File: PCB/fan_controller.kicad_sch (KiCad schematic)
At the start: 26 parts, among them IC17 LM393DR, J7 171825-2, M1 FFB0412VHN-B, Q2 SQ2348ES-T1_BE3

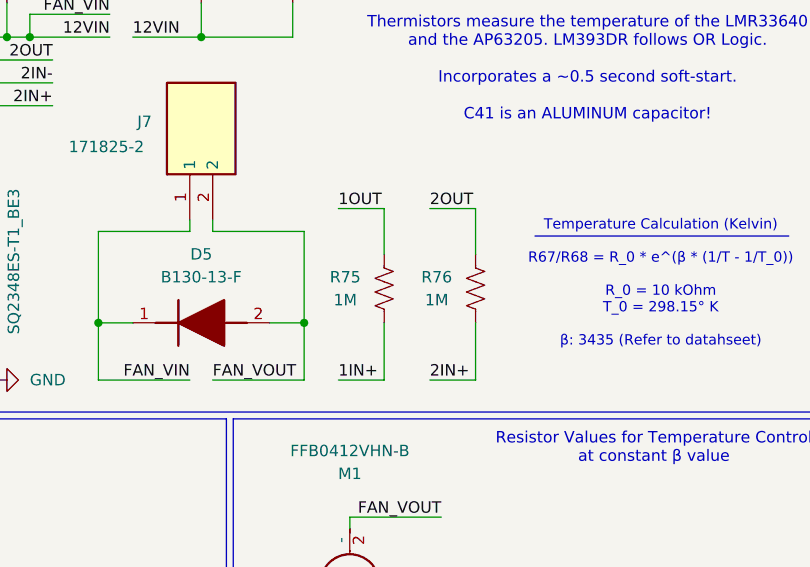
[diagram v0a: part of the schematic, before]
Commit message: Diagnosing Ethernet Controller
The Ethernet chip is dead, we'll need a new one. Minor optimizations everywhere.
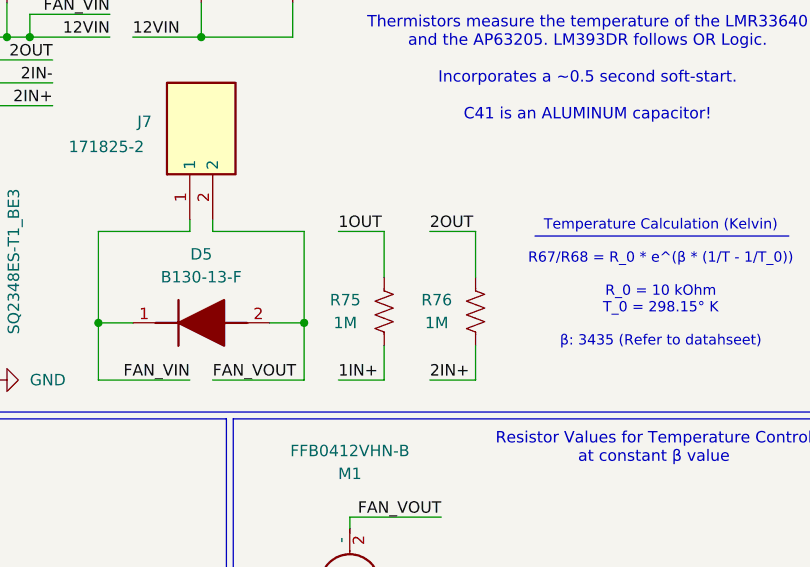
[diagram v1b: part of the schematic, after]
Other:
- moved on the sheet: R75, R76
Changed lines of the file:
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@@
 	(wire
 		(pts
-			(xy 148.59 49.53) (xy 153.67 49.53)
+			(xy 148.59 52.07) (xy 153.67 52.07)
 		)
 		(stroke
@@
 	(wire
 		(pts
-			(xy 153.67 62.23) (xy 153.67 68.58)
+			(xy 153.67 64.77) (xy 153.67 68.58)
 		)
 		(stroke
@@
 	(wire
 		(pts
-			(xy 143.51 62.23) (xy 143.51 68.58)
+			(xy 143.51 64.77) (xy 143.51 68.58)
 		)
 		(stroke
@@
 	(wire
 		(pts
-			(xy 143.51 49.53) (xy 143.51 54.61)
+			(xy 143.51 52.07) (xy 143.51 57.15)
 		)
 		(stroke
@@
 	(wire
 		(pts
-			(xy 153.67 49.53) (xy 153.67 54.61)
+			(xy 153.67 52.07) (xy 153.67 57.15)
 		)
 		(stroke
@@
 	(wire
 		(pts
-			(xy 138.43 49.53) (xy 143.51 49.53)
+			(xy 138.43 52.07) (xy 143.51 52.07)
 		)
 		(stroke
@@
 	)
 	(label "1OUT"
-		(at 138.43 49.53 0)
+		(at 138.43 52.07 0)
 		(effects
 			(font
@@
 	)
 	(label "2OUT"
-		(at 148.59 49.53 0)
+		(at 148.59 52.07 0)
 		(effects
 			(font
@@
 	(symbol
 		(lib_id "Device:R_US")
-		(at 143.51 58.42 180)
+		(at 143.51 60.96 180)
 		(unit 1)
 		(body_style 1)
@@
 		(dnp no)
 		(property "Reference" "R75"
-			(at 139.192 57.15 0)
+			(at 139.192 59.69 0)
 			(show_name no)
 			(do_not_autoplace no)
@@
 		)
 		(property "Value" "1M"
-			(at 139.192 59.69 0)
+			(at 139.192 62.23 0)
 			(show_name no)
 			(do_not_autoplace no)
@@
 		)
 		(property "Footprint" "Resistor_SMD:R_0805_2012Metric_Pad1.20x1.40mm_HandSolder"
-			(at 142.494 58.166 90)
+			(at 142.494 60.706 90)
 			(hide yes)
 			(show_name no)
@@
 		)
 		(property "Datasheet" ""
-			(at 143.51 58.42 0)
+			(at 143.51 60.96 0)
 			(hide yes)
 			(show_name no)
@@
 		)
 		(property "Description" "Resistor, US symbol"
-			(at 143.51 58.42 0)
+			(at 143.51 60.96 0)
 			(hide yes)
 			(show_name no)
@@
 		)
 		(property "Manufacturer_Part_Number" "ERA-6AEB105V "
-			(at 143.51 58.42 0)
+			(at 143.51 60.96 0)
 			(hide yes)
 			(show_name no)
@@
 		)
 		(property "Mouser Part Number" "667-ERA-6AEB105V "
-			(at 143.51 58.42 0)
+			(at 143.51 60.96 0)
 			(hide yes)
 			(show_name no)
@@
 		)
 		(property "Maunfacturer Part Number" ""
-			(at 143.51 58.42 0)
+			(at 143.51 60.96 0)
 			(hide yes)
 			(show_name no)
@@
 		)
 		(property "AVAILABILITY" ""
-			(at 143.51 58.42 0)
+			(at 143.51 60.96 0)
 			(hide yes)
 			(show_name no)
@@
 		)
 		(property "Check_prices" ""
-			(at 143.51 58.42 0)
+			(at 143.51 60.96 0)
 			(hide yes)
 			(show_name no)
@@
 		)
 		(property "MF" ""
-			(at 143.51 58.42 0)
+			(at 143.51 60.96 0)
 			(hide yes)
 			(show_name no)
@@
 		)
 		(property "MP" ""
-			(at 143.51 58.42 0)
+			(at 143.51 60.96 0)
 			(hide yes)
 			(show_name no)
@@
 		)
 		(property "Maunfacturer_Part_Number" ""
-			(at 143.51 58.42 0)
+			(at 143.51 60.96 0)
 			(hide yes)
 			(show_name no)
@@
 		)
 		(property "PACKAGE" ""
-			(at 143.51 58.42 0)
+			(at 143.51 60.96 0)
 			(hide yes)
 			(show_name no)
@@
 		)
 		(property "PARTREV" ""
-			(at 143.51 58.42 0)
+			(at 143.51 60.96 0)
 			(hide yes)
 			(show_name no)
@@
 		)
 		(property "PRICE" ""
-			(at 143.51 58.42 0)
+			(at 143.51 60.96 0)
 			(hide yes)
 			(show_name no)
@@
 		)
 		(property "STANDARD" ""
-			(at 143.51 58.42 0)
+			(at 143.51 60.96 0)
 			(hide yes)
 			(show_name no)
@@
 		)
 		(property "SnapEDA_Link" ""
-			(at 143.51 58.42 0)
+			(at 143.51 60.96 0)
 			(hide yes)
 			(show_name no)
@@
 	(symbol
 		(lib_id "Device:R_US")
-		(at 153.67 58.42 180)
+		(at 153.67 60.96 180)
 		(unit 1)
 		(body_style 1)
@@
 		(dnp no)
 		(property "Reference" "R76"
-			(at 149.352 57.15 0)
+			(at 149.352 59.69 0)
 			(show_name no)
 			(do_not_autoplace no)
@@
 		)
 		(property "Value" "1M"
-			(at 149.352 59.69 0)
+			(at 149.352 62.23 0)
 			(show_name no)
 			(do_not_autoplace no)
@@
 		)
 		(property "Footprint" "Resistor_SMD:R_0805_2012Metric_Pad1.20x1.40mm_HandSolder"
-			(at 152.654 58.166 90)
+			(at 152.654 60.706 90)
 			(hide yes)
 			(show_name no)
@@
 		)
 		(property "Datasheet" ""
-			(at 153.67 58.42 0)
+			(at 153.67 60.96 0)
 			(hide yes)
 			(show_name no)
@@
 		)
 		(property "Description" "Resistor, US symbol"
-			(at 153.67 58.42 0)
+			(at 153.67 60.96 0)
 			(hide yes)
 			(show_name no)
@@
 		)
 		(property "Manufacturer_Part_Number" "ERA-6AEB105V "
-			(at 153.67 58.42 0)
+			(at 153.67 60.96 0)
 			(hide yes)
 			(show_name no)
@@
 		)
 		(property "Mouser Part Number" "667-ERA-6AEB105V "
-			(at 153.67 58.42 0)
+			(at 153.67 60.96 0)
 			(hide yes)
 			(show_name no)
@@
 		)
 		(property "Maunfacturer Part Number" ""
-			(at 153.67 58.42 0)
+			(at 153.67 60.96 0)
 			(hide yes)
 			(show_name no)
@@
 		)
 		(property "AVAILABILITY" ""
-			(at 153.67 58.42 0)
+			(at 153.67 60.96 0)
 			(hide yes)
 			(show_name no)
@@
 		)
 		(property "Check_prices" ""
-			(at 153.67 58.42 0)
+			(at 153.67 60.96 0)
 			(hide yes)
 			(show_name no)
@@
 		)
 		(property "MF" ""
-			(at 153.67 58.42 0)
+			(at 153.67 60.96 0)
 			(hide yes)
 			(show_name no)
@@
 		)
 		(property "MP" ""
-			(at 153.67 58.42 0)
+			(at 153.67 60.96 0)
 			(hide yes)
 			(show_name no)
@@
 		)
 		(property "Maunfacturer_Part_Number" ""
-			(at 153.67 58.42 0)
+			(at 153.67 60.96 0)
 			(hide yes)
 			(show_name no)
@@
 		)
 		(property "PACKAGE" ""
-			(at 153.67 58.42 0)
+			(at 153.67 60.96 0)
 			(hide yes)
 			(show_name no)
@@
 		)
 		(property "PARTREV" ""
-			(at 153.67 58.42 0)
+			(at 153.67 60.96 0)
 			(hide yes)
 			(show_name no)
@@
 		)
 		(property "PRICE" ""
-			(at 153.67 58.42 0)
+			(at 153.67 60.96 0)
 			(hide yes)
 			(show_name no)
@@
 		)
 		(property "STANDARD" ""
-			(at 153.67 58.42 0)
+			(at 153.67 60.96 0)
 			(hide yes)
 			(show_name no)
@@
 		)
 		(property "SnapEDA_Link" ""
-			(at 153.67 58.42 0)
+			(at 153.67 60.96 0)
 			(hide yes)
 			(show_name no)

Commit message: Updated PDF schematic, tweaked connections
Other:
- moved on the sheet: D4, R68, RT1
